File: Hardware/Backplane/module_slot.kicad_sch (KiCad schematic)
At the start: 37 parts, among them J401 Conn_01x10, J402 10018784-10201TLF, J403 Conn_01x06, Q401 S3134K, Q402 GSF3407, Q403 GSF3407, Q404 GSF3407

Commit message: Adjusts to review comments
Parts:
- removed C402, C404, C406: 1u, symbol Device:C_Polarized
- added R413: 270, Resistor_SMD:R_0603_1608Metric, symbol Device:R
- C401: footprint (none) -> Capacitor_SMD:C_0603_1608Metric
- C403, C405: footprint (none) -> Capacitor_SMD:C_0603_1608Metric; Digikey Part No (none) -> 490-13247-1-ND
- F401, F402, F403: footprint (none) -> Fuse:Fuse_1206_3216Metric; Digikey Part No (none) -> 13-SMD1206B050TF/15TR-ND
- J401: Digikey Part No (none) -> WM1739-ND
- J403: Digikey Part No (none) -> WM1735-ND
- R401: value 1K -> 0; Digikey Part No (none) -> 311-0.0GRCT-ND
- R402, R403, R404, R405: Digikey Part No (none) -> 311-0.0GRCT-ND
- R406, R407, R408, R409, R410: value 4K7 -> 10K; Digikey Part No (none) -> 311-10.0KHRCT-ND
- R411: value TODO -> 10K; Digikey Part No (none) -> 311-10.0KHRCT-ND
- R412: footprint (none) -> Resistor_SMD:R_0603_1608Metric; Digikey Part No (none) -> RMCF0603FT270RCT-ND
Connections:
- net MOD_+12V: now also Q402.1 (D); no longer Q402.3 (S)
- net MOD_+3V3: now also Q404.1 (D); no longer Q404.3 (S)
- net MOD_+5V: now also Q403.1 (D); no longer Q403.3 (S)
- net POWER_ON: now also R413.2; no longer Q401.2 (G)
- net at F403.1: now also Q404.3 (S); no longer Q404.1 (D)
- net at F402.1: now also Q403.3 (S); no longer Q403.1 (D)
- net at F401.1: now also Q402.3 (S); no longer Q402.1 (D)
- new net: Q401.2 (G), R413.1
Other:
- note added: "TODO: Elko"

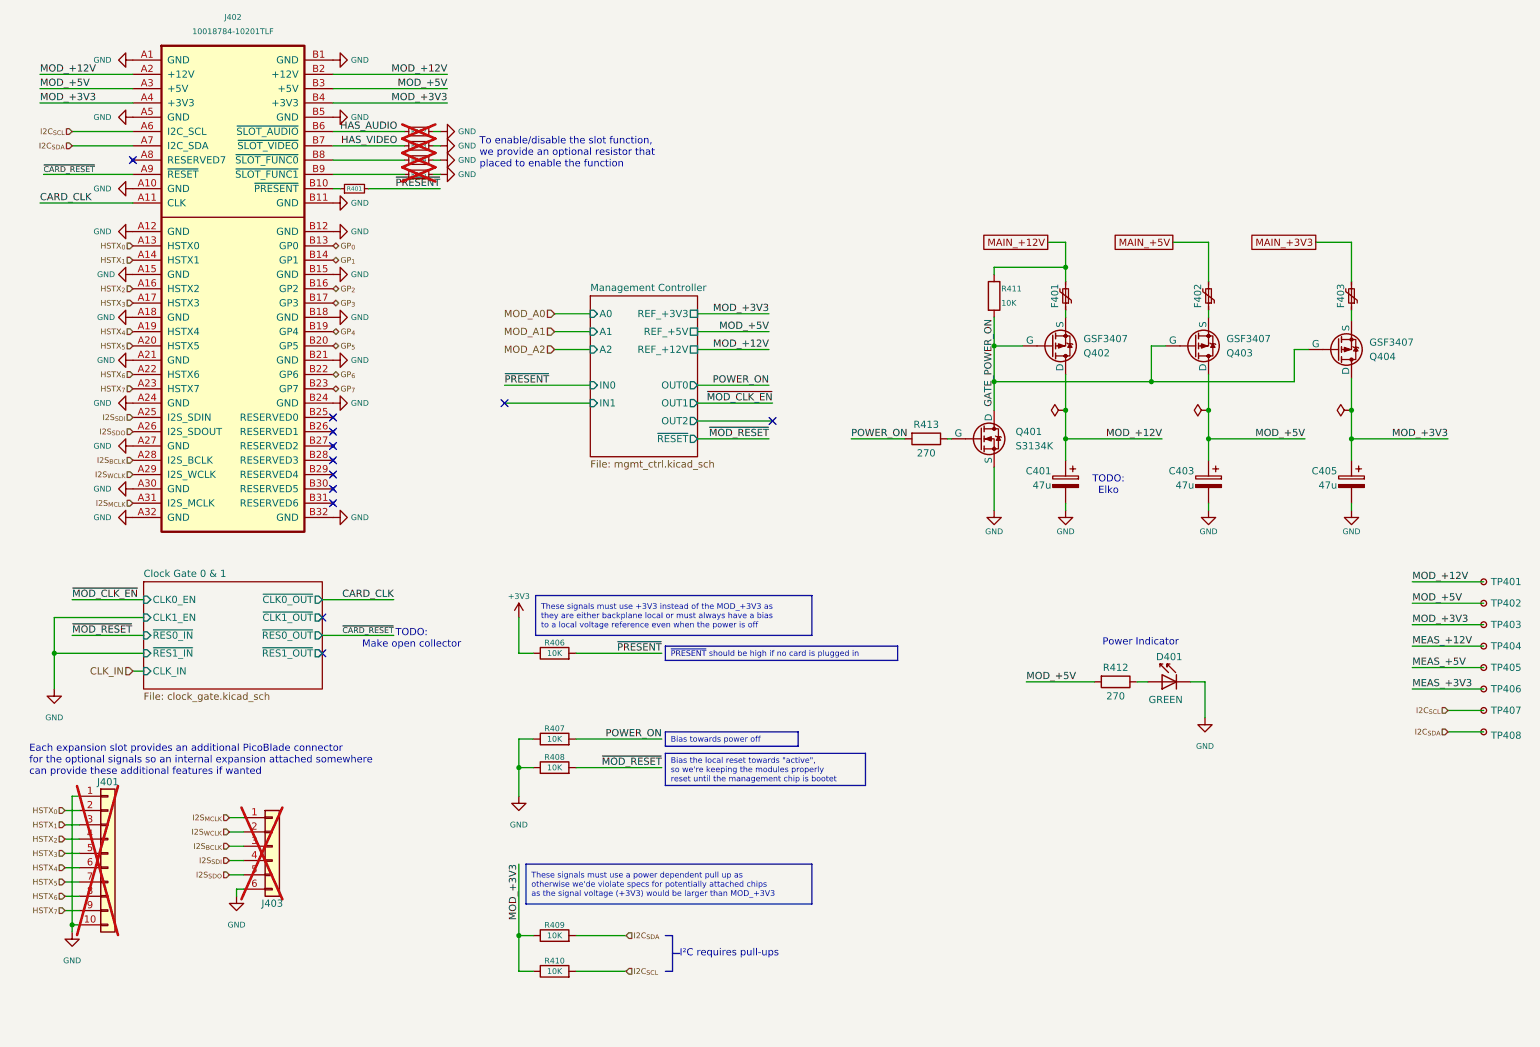
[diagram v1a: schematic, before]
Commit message: Starts refactoring Backplane to use NL17SZS11-D instead of 4-port AND
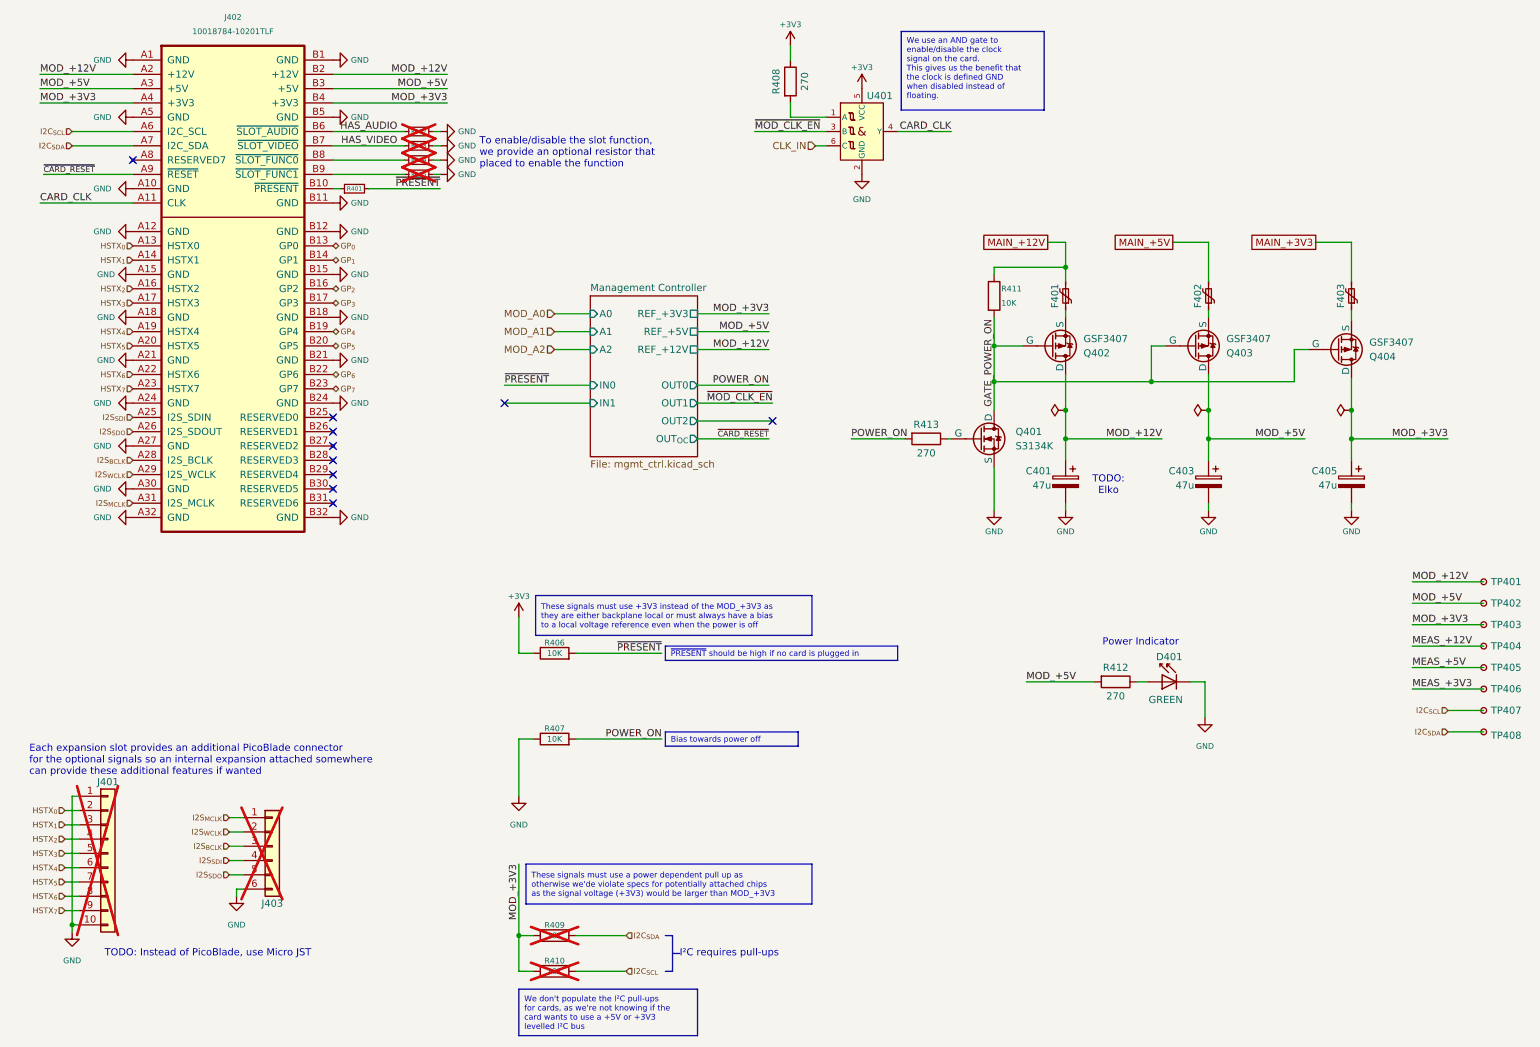
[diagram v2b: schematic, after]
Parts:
- added U401: NL17SZS11DFT2G-Q, Package_TO_SOT_SMD:SOT-363_SC-70-6, symbol Home Computer:NL17SZS11DFT2G-Q
- R408: value 10K -> 270; Digikey Part No 311-10.0KHRCT-ND -> RMCF0603FT270RCT-ND
- R409, R410: now not fitted
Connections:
- net +3V3: now also R408.1, U401.5 (VCC)
- net CARD_CLK: now also U401.4 (Y)
- net CLK_IN: now also U401.6 (C)
- net GND: now also U401.2 (GND); no longer R408.1
- net ~{MOD_CLK_EN}: now also U401.3 (B)
- net ~{MOD_RESET}: no longer names the net of R408.2
- net ~{MOD_RESET}: now also U401.1 (A)
- no-connect marks 12 -> 10
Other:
- removed sheet Clock Gate 0 & 1
- sheet Management Controller ports: added OUT_{OC}; removed ~{RESET}
- note added: "TODO: Instead of PicoBlade, use Micro JST"
- note removed: "TODO: Make open collector"

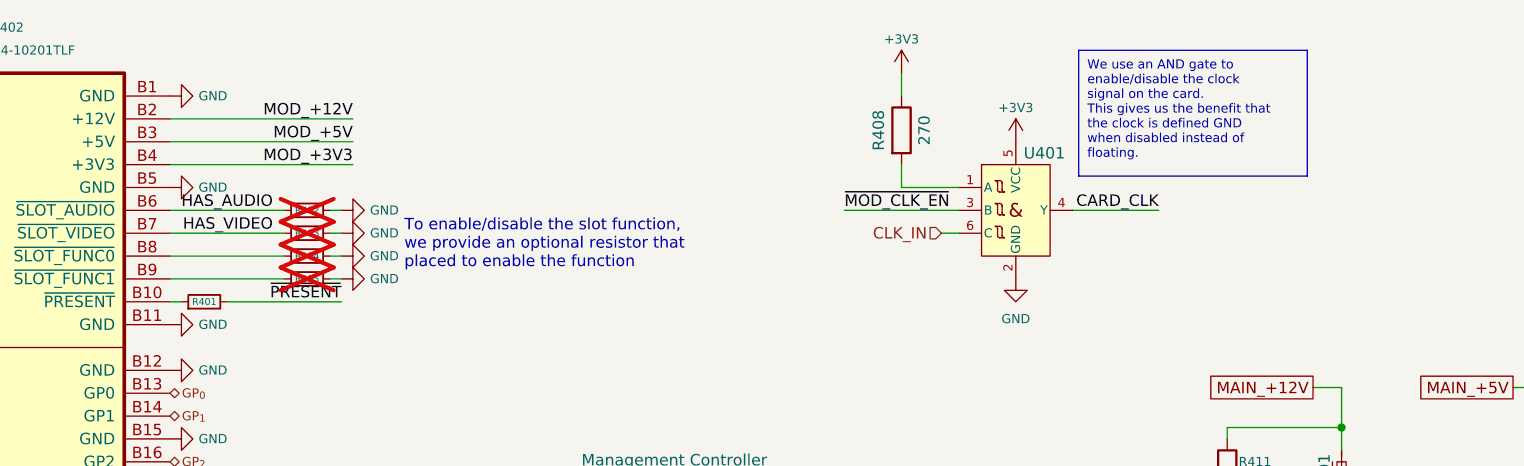
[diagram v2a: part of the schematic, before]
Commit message: Cleans up Backplane schematic even more. Less parts in the BOM, less mistakes!
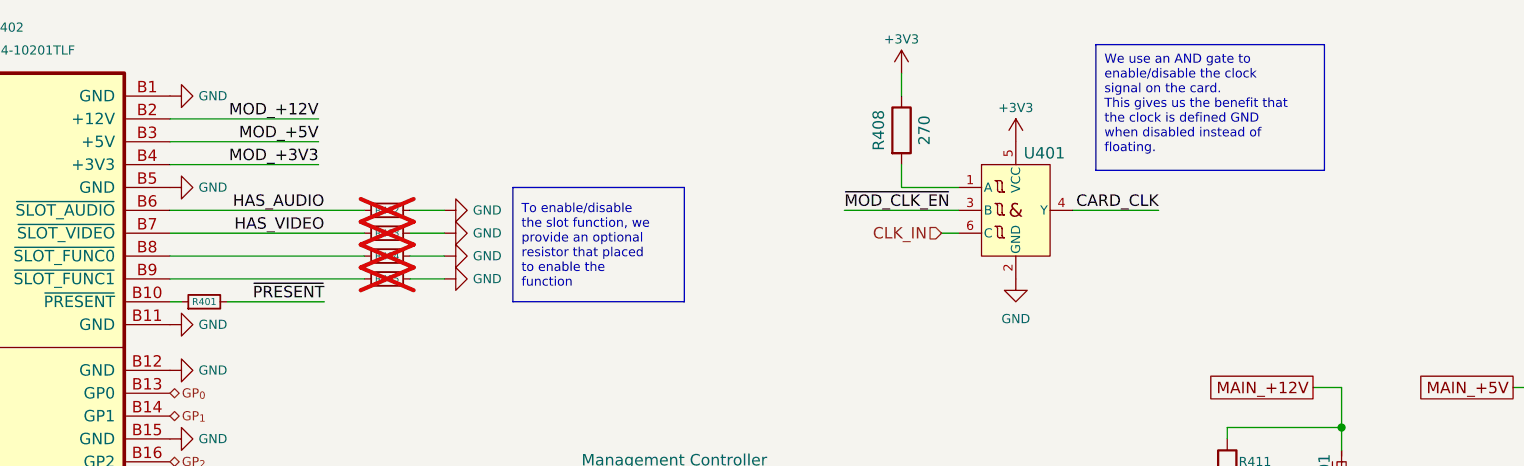
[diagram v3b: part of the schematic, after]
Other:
- note removed: "To enable/disable the slot function, we provide an optional resistor that placed to enable the function"
- moved on the sheet: R402, R403, R404, R405
